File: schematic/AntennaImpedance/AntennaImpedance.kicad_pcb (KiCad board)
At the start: 2 copper layers, 90.3 x 96.1 mm, 12 parts, among them J1 RF_Source, J2 RF_Source

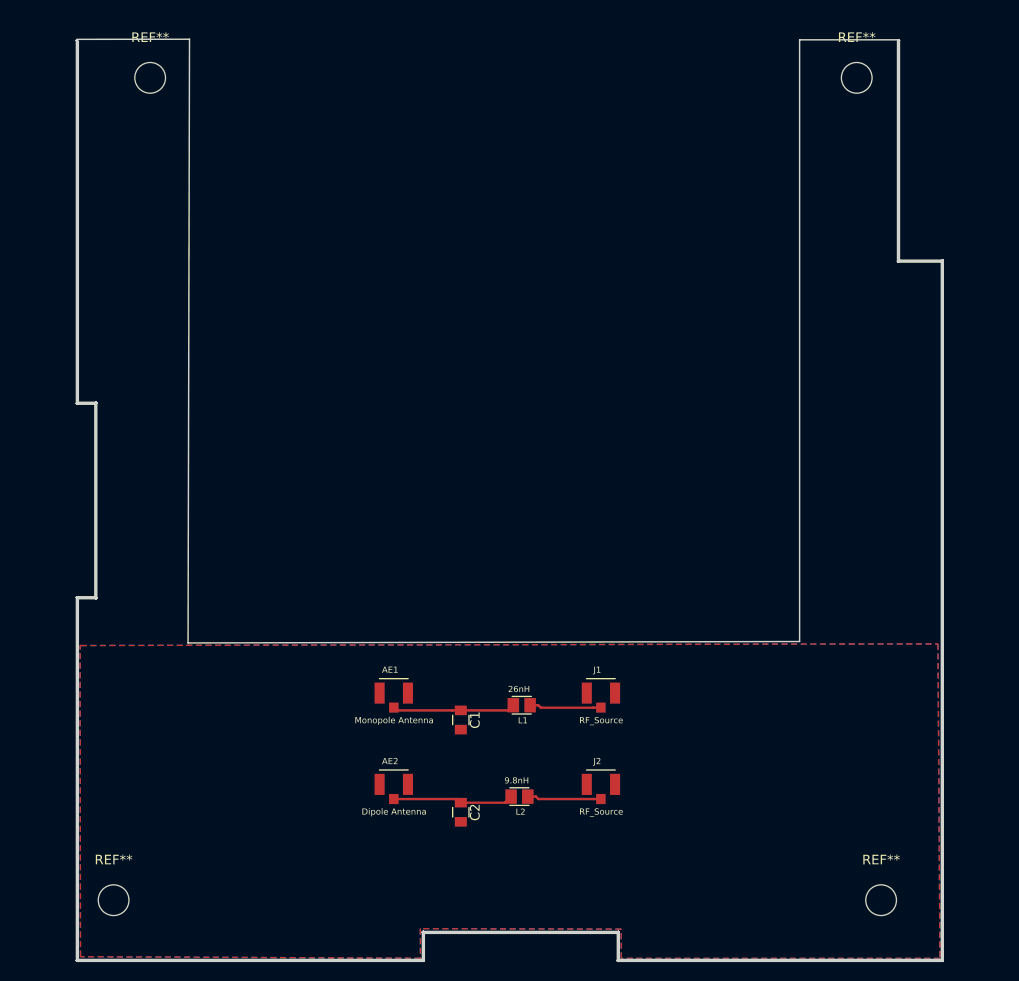
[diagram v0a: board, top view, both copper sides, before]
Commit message: Added to the silkscreen
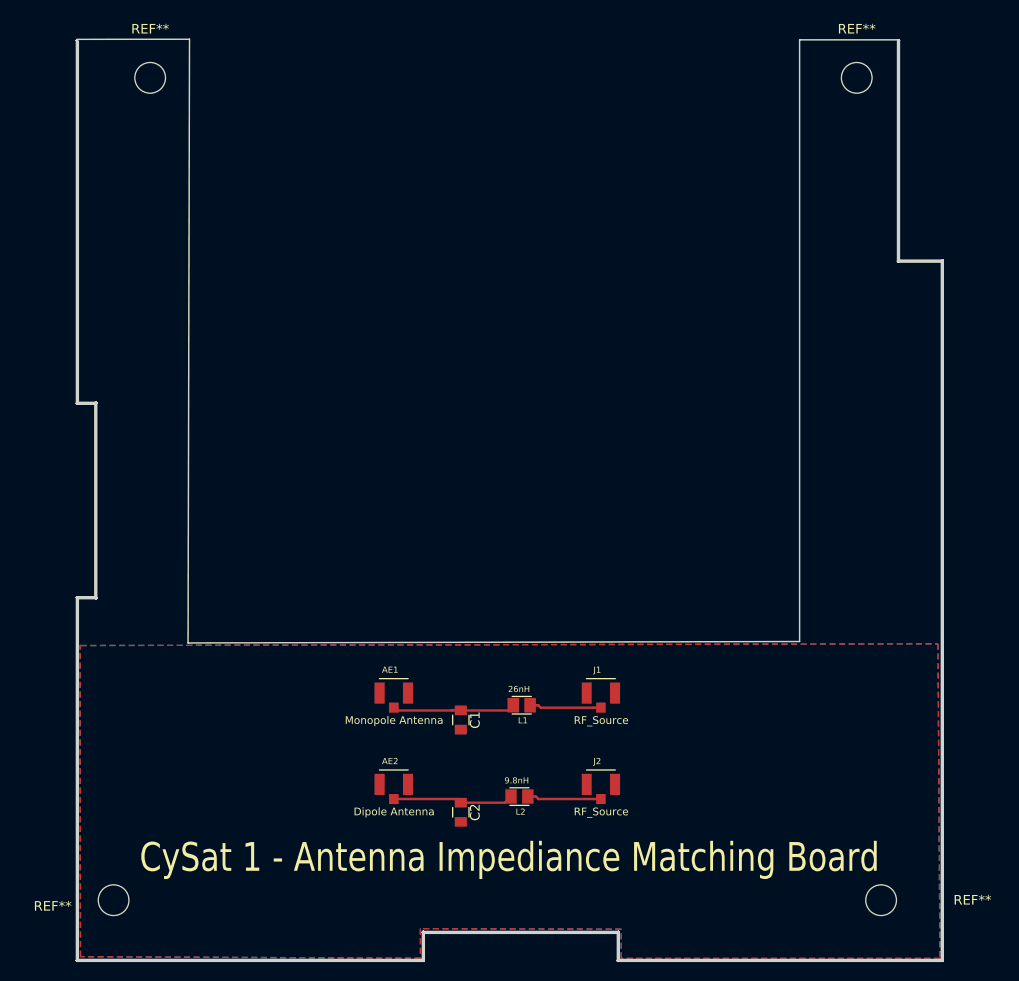
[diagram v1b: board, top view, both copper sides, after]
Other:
- board text added: "CySat 1 - Antenna Impediance Matching Board"
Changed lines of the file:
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@@
   (general
     (thickness 1.6)
-    (drawings 278)
+    (drawings 279)
     (tracks 18)
     (zones 0)
@@
     (tags "mounting hole 3.2mm no annular m3")
     (attr virtual)
-    (fp_text reference REF** (at 0 -4.2) (layer F.SilkS)
+    (fp_text reference REF** (at 0 -5.08) (layer F.SilkS)
       (effects (font (size 1 1) (thickness 0.15)))
     )
@@
     (tags "mounting hole 3.2mm no annular m3")
     (attr virtual)
-    (fp_text reference REF** (at 0 -4.2) (layer F.SilkS)
+    (fp_text reference REF** (at 0 -5.08) (layer F.SilkS)
       (effects (font (size 1 1) (thickness 0.15)))
     )
@@
     (tags "mounting hole 3.2mm no annular m3")
     (attr virtual)
-    (fp_text reference REF** (at 0 -4.2) (layer F.SilkS)
+    (fp_text reference REF** (at -6.35 0.63) (layer F.SilkS)
       (effects (font (size 1 1) (thickness 0.15)))
     )
@@
     (tags "mounting hole 3.2mm no annular m3")
     (attr virtual)
-    (fp_text reference REF** (at 0 -4.2) (layer F.SilkS)
+    (fp_text reference REF** (at 9.525 -0.005) (layer F.SilkS)
       (effects (font (size 1 1) (thickness 0.15)))
     )
@@
     )
     (fp_text value "Monopole Antenna" (at 0.032067 2.84966) (layer F.SilkS)
-      (effects (font (size 0.641364 0.641364) (thickness 0.05)))
+      (effects (font (size 0.8 0.8) (thickness 0.1)))
     )
     (fp_line (start -1.5 -1.5) (end 1.5 -1.5) (layer F.SilkS) (width 0.127))
@@
     )
     (fp_text value "Dipole Antenna" (at 0.032067 2.84966) (layer F.SilkS)
-      (effects (font (size 0.641364 0.641364) (thickness 0.05)))
+      (effects (font (size 0.8 0.8) (thickness 0.1)))
     )
     (fp_line (start -1.5 -1.5) (end 1.5 -1.5) (layer F.SilkS) (width 0.127))
@@
     )
     (fp_text value RF_Source (at 0.032067 2.84966) (layer F.SilkS)
-      (effects (font (size 0.641364 0.641364) (thickness 0.05)))
+      (effects (font (size 0.8 0.8) (thickness 0.1)))
     )
     (fp_line (start -2.25 2.28) (end -2.25 -1.75) (layer Eco1.User) (width 0.05))
@@
     )
     (fp_text value RF_Source (at 0.032067 2.84966) (layer F.SilkS)
-      (effects (font (size 0.641364 0.641364) (thickness 0.05)))
+      (effects (font (size 0.8 0.8) (thickness 0.1)))
     )
     (fp_line (start -2.25 2.28) (end -2.25 -1.75) (layer Eco1.User) (width 0.05))
@@
       (net 3 "Net-(AE2-Pad1)"))
   )
+  (gr_text "CySat 1 - Antenna Impediance Matching Board" (at 150.495 134.62) (layer F.SilkS)
+    (effects (font (size 3 2.4) (thickness 0.3)))
+  )
   (gr_line (start 117.1321 49.3141) (end 105.41 49.3268) (layer Edge.Cuts) (width 0.15))
